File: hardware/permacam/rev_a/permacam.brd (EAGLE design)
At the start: 27 x 60 mm, 111 parts, among them J1 TC2030-JLINK-NL, Q1 PMDXB950UPEL, Q2 PMDXB950UPEL, Q3 PMDXB950UPEL, Q4 PMDXB950UPEL, Q5 PMDXB950UPEL, Q6 PMDXB950UPEL, U1 AB1815-T3, U10 NRF52840, U2 BQ25505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

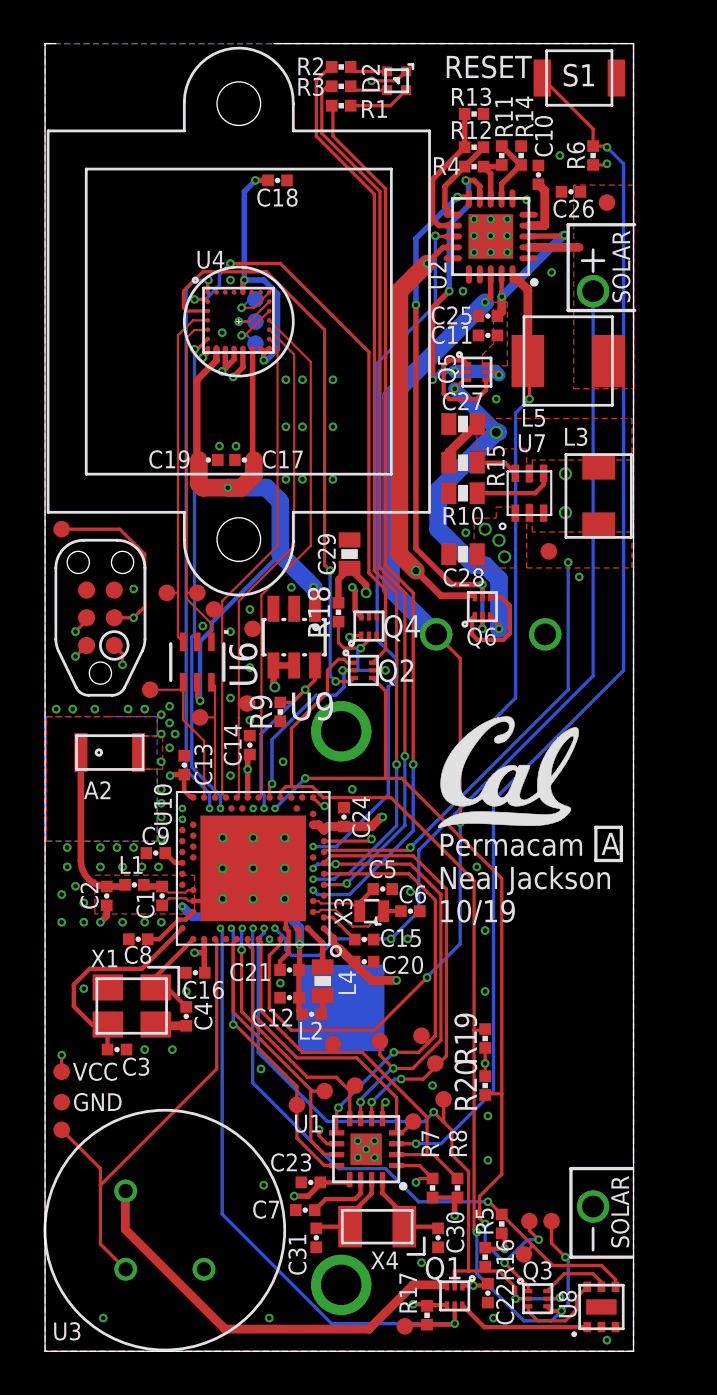
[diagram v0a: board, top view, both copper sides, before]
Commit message: Holes for 18mm holders
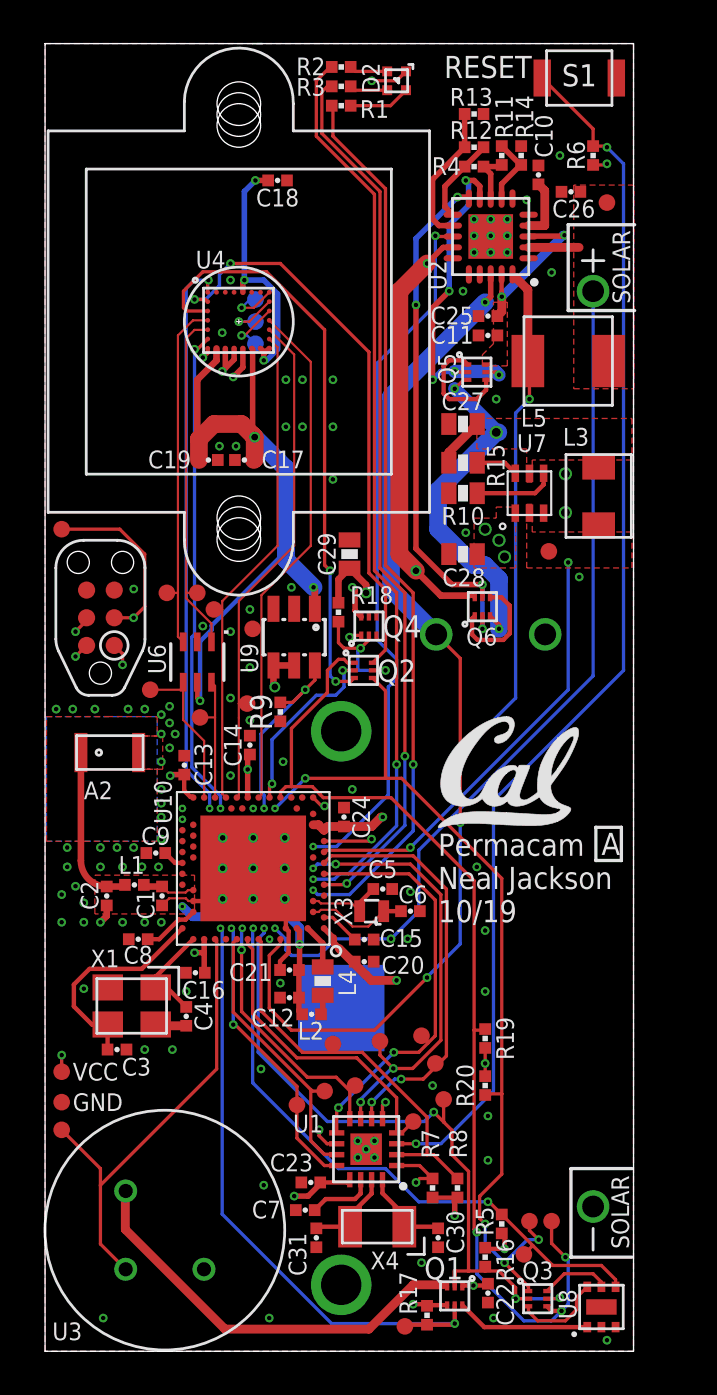
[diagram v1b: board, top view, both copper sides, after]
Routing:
- net GND: vias 115 -> 113
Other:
- outline, holes or cut-outs redrawn
